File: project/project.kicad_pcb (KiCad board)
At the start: 2 copper layers, 51.2 x 76.5 mm, 15 parts, among them J1 Conn_01x02_Socket, SW1 SW_Push_45deg, SW2 SW_Push_45deg, SW3 SW_Push_45deg

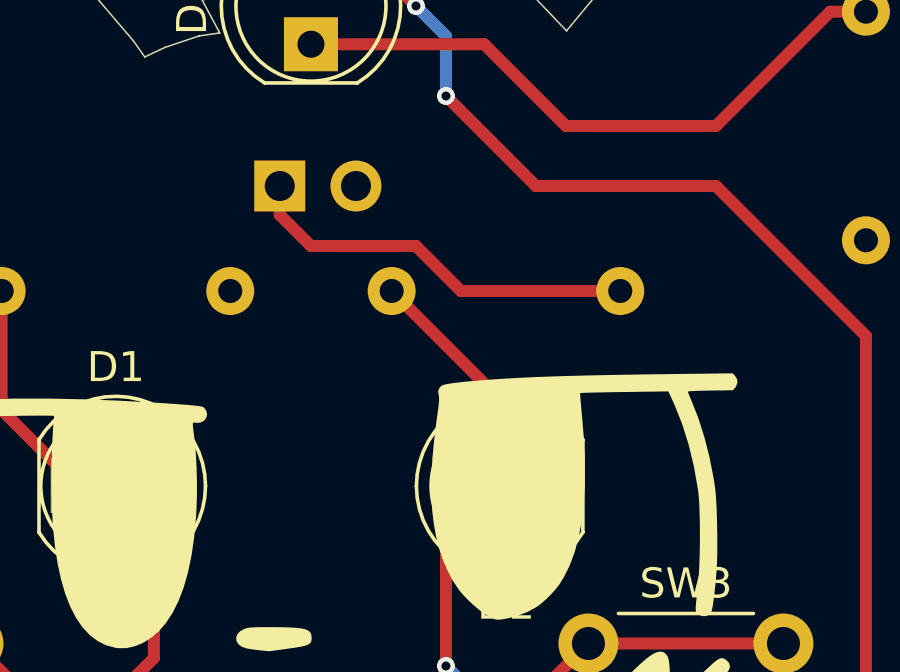
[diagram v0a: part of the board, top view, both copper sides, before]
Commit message: Put component in parallel
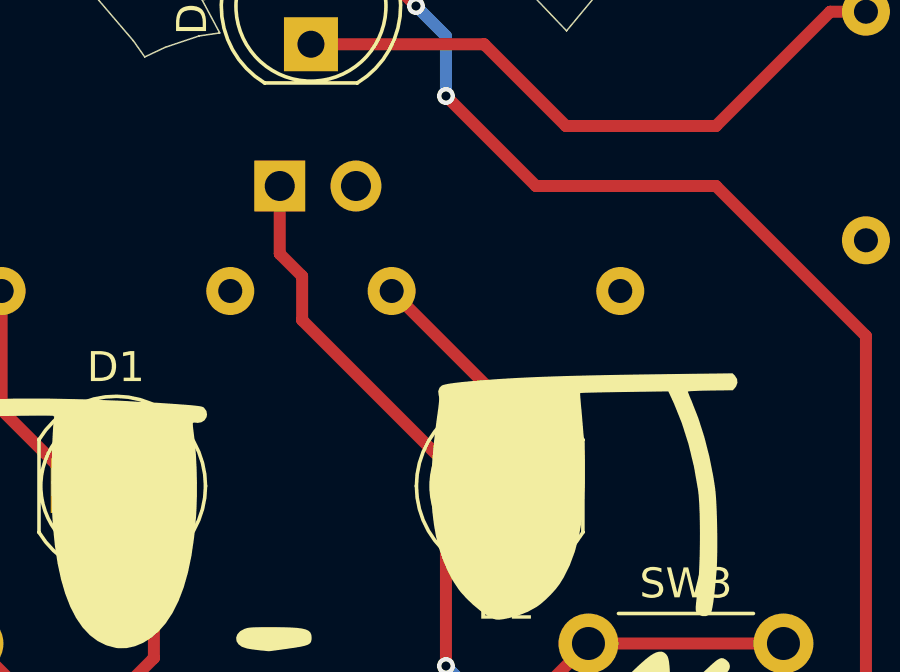
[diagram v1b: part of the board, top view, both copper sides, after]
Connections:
- J1 pad 1: Net-(J1-Pin_1) -> Net-(D2-A)
- R2 pad 2: Net-(J1-Pin_1) -> GND
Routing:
- net Net-(J1-Pin_1): track 13.4 -> 0.00 mm
- net Net-(D2-A): track 24.6 -> 37.2 mm
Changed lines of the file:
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@@
 	(net 7 "Net-(D3-A)")
 	(net 8 "Net-(D3-K)")
-	(net 9 "Net-(J1-Pin_1)")
 	(footprint "LED_THT:LED_D5.0mm"
 		(layer "F.Cu")
@@
 			(layers "*.Cu" "*.Mask")
 			(remove_unused_layers no)
-			(net 9 "Net-(J1-Pin_1)")
+			(net 2 "GND")
 			(pintype "passive")
 		)
@@
 			(layers "*.Cu" "*.Mask")
 			(remove_unused_layers no)
-			(net 9 "Net-(J1-Pin_1)")
+			(net 6 "Net-(D2-A)")
 			(pinfunction "Pin_1")
 			(pintype "passive")
@@
 	)
 	(segment
+		(start 126.20625 50.00625)
+		(end 125.46 49.26)
+		(width 0.4)
+		(layer "F.Cu")
+		(net 6)
+	)
+	(segment
+		(start 126.20625 51.47125)
+		(end 126.20625 50.00625)
+		(width 0.4)
+		(layer "F.Cu")
+		(net 6)
+	)
+	(segment
 		(start 122.75 73.25)
 		(end 129.25 73.25)
@@
 	)
 	(segment
+		(start 131.735 57)
+		(end 126.20625 51.47125)
+		(width 0.4)
+		(layer "F.Cu")
+		(net 6)
+	)
+	(segment
 		(start 131 63)
 		(end 131 57.735)
@@
 	)
 	(segment
+		(start 125.46 49.26)
+		(end 125.46 47)
+		(width 0.4)
+		(layer "F.Cu")
+		(net 6)
+	)
+	(segment
 		(start 131 57.735)
 		(end 131.735 57)
@@
 		(net 8)
 	)
-	(segment
-		(start 125.46 47.96)
-		(end 125.46 47)
-		(width 0.4)
-		(layer "F.Cu")
-		(net 9)
-	)
-	(segment
-		(start 131.5 50.5)
-		(end 130 49)
-		(width 0.4)
-		(layer "F.Cu")
-		(net 9)
-	)
-	(segment
-		(start 130 49)
-		(end 126.5 49)
-		(width 0.4)
-		(layer "F.Cu")
-		(net 9)
-	)
-	(segment
-		(start 136.81 50.5)
-		(end 131.5 50.5)
-		(width 0.4)
-		(layer "F.Cu")
-		(net 9)
-	)
-	(segment
-		(start 126.5 49)
-		(end 125.46 47.96)
-		(width 0.4)
-		(layer "F.Cu")
-		(net 9)
-	)
 	(zone
